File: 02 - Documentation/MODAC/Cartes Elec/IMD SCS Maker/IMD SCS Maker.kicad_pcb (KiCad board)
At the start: 2 copper layers, 32 x 22.4 mm, 12 parts, among them J1 2P Droit 2-11-2022, J3 3P Droit 22-11-2032, Q1 NMOS SQ2348ES-T1_GE3, U1 Alim LP TSR_0.5-2450

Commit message: MAJ 3D Modac
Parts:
- moved J1 2.31 mm to (67.3, 54.4), turned to -90 degrees
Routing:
- net +12V: track 17.2 -> 19.3 mm
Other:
- board text added: "12V"
- board text added: "GND"
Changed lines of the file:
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@@
 			(layer "F.Fab")
 		)
+		(fp_text user "${REFERENCE}"
+			(at -2.54 0 0)
+			(layer "F.Fab")
+			(effects
+				(font
+					(size 1.27 1.27)
+					(thickness 0.254)
+				)
+			)
+		)
 		(pad "1" thru_hole circle
 			(at 3.21 -2)
@@
 			(pintype "passive")
 		)
-		(model "TSR_0.5-2450.stp"
+		(model "${EPSA3D}/TSR_0.5-2450.stp"
 			(offset
 				(xyz -21.61000029 17.88999912 10.24999985)
@@
 			(pintype "passive")
 		)
-		(model "22-11-2032.step"
+		(model "${EPSA3D}/22-11-2032.step"
 			(offset
 				(xyz 2.54 0 1.5)
@@
 	(footprint "EPSA_lib:MOLEX_22-11-2022"
 		(layer "F.Cu")
-		(at 67.3165 56.706 90)
+		(at 67.3165 54.4 -90)
 		(property "Reference" "J1"
-			(at 1.488 -2.1 -90)
+			(at 1.488 -2.1 90)
 			(layer "F.SilkS")
 			(effects
@@
 		)
 		(property "Value" "2P Droit 2-11-2022"
-			(at 7.62 4.615 -90)
+			(at 7.62 4.615 90)
 			(layer "F.Fab")
 			(effects
@@
 		)
 		(property "Footprint" "EPSA_lib:MOLEX_22-11-2022"
-			(at 0 0 90)
+			(at 0 0 -90)
 			(unlocked yes)
 			(layer "F.Fab")
@@
 		)
 		(property "Datasheet" ""
-			(at 0 0 90)
+			(at 0 0 -90)
 			(unlocked yes)
 			(layer "F.Fab")
@@
 		)
 		(property "Description" ""
-			(at 0 0 90)
+			(at 0 0 -90)
 			(unlocked yes)
 			(layer "F.Fab")
@@
 		)
 		(property "Sim.Pins" "1=1 2=2"
-			(at 0 0 90)
+			(at 0 0 -90)
 			(unlocked yes)
 			(layer "F.Fab")
@@
 		)
 		(property "Sim.Device" "SPICE"
-			(at 0 0 90)
+			(at 0 0 -90)
 			(unlocked yes)
 			(layer "F.Fab")
@@
 		)
 		(property "Sim.Params" "type=\"J\" model=\"22-11-2022\" lib=\"\""
-			(at 0 0 90)
+			(at 0 0 -90)
 			(unlocked yes)
 			(layer "F.Fab")
@@
 		)
 		(property "MAXIMUM_PACKAGE_HEIGHT" "10.66mm"
-			(at 0 0 90)
+			(at 0 0 -90)
 			(unlocked yes)
 			(layer "F.Fab")
@@
 		)
 		(property "PARTREV" "BD8"
-			(at 0 0 90)
+			(at 0 0 -90)
 			(unlocked yes)
 			(layer "F.Fab")
@@
 		)
 		(property "STANDARD" "Manufacturer Recommendations"
-			(at 0 0 90)
+			(at 0 0 -90)
 			(unlocked yes)
 			(layer "F.Fab")
@@
 		)
 		(property "MANUFACTURER" "Molex"
-			(at 0 0 90)
+			(at 0 0 -90)
 			(unlocked yes)
 			(layer "F.Fab")
@@
 		)
 		(property "Render Name" "2P Droit"
-			(at 0 0 90)
+			(at 0 0 -90)
 			(unlocked yes)
 			(layer "F.Fab")
@@
 		(attr through_hole)
 		(fp_line
-			(start 3.735 -3.1)
-			(end 3.735 3.25)
+			(start -1.195 3.25)
+			(end -1.195 -3.1)
 			(stroke
 				(width 0.127)
@@
 		)
 		(fp_line
-			(start -1.195 -3.1)
-			(end 3.735 -3.1)
+			(start 3.735 3.25)
+			(end -1.195 3.25)
 			(stroke
 				(width 0.127)
@@
 		)
 		(fp_line
-			(start 3.735 3.25)
-			(end -1.195 3.25)
+			(start -1.195 -3.1)
+			(end 3.735 -3.1)
 			(stroke
 				(width 0.127)
@@
 		)
 		(fp_line
-			(start -1.195 3.25)
-			(end -1.195 -3.1)
+			(start 3.735 -3.1)
+			(end 3.735 3.25)
 			(stroke
 				(width 0.127)
@@
 		)
 		(fp_line
-			(start 3.985 -3.35)
-			(end 3.985 3.5)
+			(start -1.445 3.5)
+			(end -1.445 -3.35)
 			(stroke
 				(width 0.05)
@@
 		)
 		(fp_line
-			(start -1.445 -3.35)
-			(end 3.985 -3.35)
+			(start 3.985 3.5)
+			(end -1.445 3.5)
 			(stroke
 				(width 0.05)
@@
 		)
 		(fp_line
-			(start 3.985 3.5)
-			(end -1.445 3.5)
+			(start -1.445 -3.35)
+			(end 3.985 -3.35)
 			(stroke
 				(width 0.05)
@@
 		)
 		(fp_line
-			(start -1.445 3.5)
-			(end -1.445 -3.35)
+			(start 3.985 -3.35)
+			(end 3.985 3.5)
 			(stroke
 				(width 0.05)
@@
 		)
 		(fp_line
-			(start 3.735 -3.1)
-			(end 3.735 3.25)
+			(start -1.195 3.25)
+			(end -1.195 -3.1)
 			(stroke
 				(width 0.127)
@@
 		)
 		(fp_line
-			(start -1.195 -3.1)
-			(end 3.735 -3.1)
+			(start 3.735 3.25)
+			(end -1.195 3.25)
 			(stroke
 				(width 0.127)
@@
 		)
 		(fp_line
-			(start 3.735 3.25)
-			(end -1.195 3.25)
+			(start -1.195 -3.1)
+			(end 3.735 -3.1)
 			(stroke
 				(width 0.127)
@@
 		)
 		(fp_line
-			(start -1.195 3.25)
-			(end -1.195 -3.1)
+			(start 3.735 -3.1)
+			(end 3.735 3.25)
 			(stroke
 				(width 0.127)
@@
 		)
 		(pad "1" thru_hole rect
-			(at 0 0 90)
+			(at 0 0 270)
 			(size 1.53 1.53)
 			(drill 1.02)
@@
 		)
 		(pad "2" thru_hole circle
-			(at 2.54 0 90)
+			(at 2.54 0 270)
 			(size 1.53 1.53)
 			(drill 1.02)
@@
 			(pintype "passive")
 		)
-		(model "22-11-2022.step"
+		(model "${EPSA3D}/22-11-2022.step"
 			(offset
 				(xyz 1.25 0 1.5)
@@
 			(pintype "passive")
 		)
-		(model "RK73H2BLTDD2152F.stp"
+		(model "${EPSA3D}/RK73H2BLTDD2152F.stp"
 			(offset
 				(xyz 0 0 0)
@@
 			(pintype "passive")
 		)
-		(model "RK73H2BLTDD2152F.stp"
+		(model "${EPSA3D}/RK73H2BLTDD2152F.stp"
 			(offset
 				(xyz 0 0 0)
@@
 			(pintype "passive")
 		)
-		(model "0805Y1000104JXT.stp"
+		(model "${EPSA3D}/0805Y1000104JXT.stp"
 			(offset
 				(xyz 0 0 0)
@@
 		(tags "MOSFET (P-Channel)")
 		(property "Reference" "Q1"
-			(at 1.05 -2.730562 360)
+			(at 1.05 -2.730562 0)
 			(layer "F.SilkS")
 			(effects
@@
 		)
 		(property "Value" "NMOS SQ2348ES-T1_GE3"
-			(at -0.05 5.08 360)
+			(at -0.05 5.08 0)
 			(layer "F.SilkS")
 			(hide yes)
@@
 		)
 		(fp_text user "${REFERENCE}"
-			(at -5.08 0 360)
+			(at -5.08 0 0)
 			(layer "F.Fab")
 			(effects
@@
 			(pintype "passive")
 		)
-		(model "${EPSA}/3Dmodel/SI2343CDS-T1-GE3.stp"
+		(model "${EPSA3D}/SI2343CDS-T1-GE3.stp"
 			(offset
 				(xyz 0 0 0)
@@
 			(pintype "passive")
 		)
-		(model "RK73H2BLTDD2152F.stp"
+		(model "${EPSA3D}/RK73H2BLTDD2152F.stp"
 			(offset
 				(xyz 0 0 0)
@@
 		(layer "Edge.Cuts")
 	)
+	(gr_text "GND"
+		(at 64.2 53 0)
+		(layer "F.SilkS")
+		(effects
+			(font
+				(size 0.7 0.7)
+				(thickness 0.175)
+				(bold yes)
+			)
+			(justify left bottom)
+		)
+	)
 	(gr_text "SCS Maker V1.0 EPSA"
 		(at 67.7565 60.96 0)
@@
 		)
 	)
+	(gr_text "12V"
+		(at 64.2 59.4 0)
+		(layer "F.SilkS")
+		(effects
+			(font
+				(size 0.7 0.7)
+				(thickness 0.175)
+				(bold yes)
+			)
+			(justify left bottom)
+		)
+	)
 	(segment
-		(start 67.595388 56.427112)
-		(end 67.3165 56.706)
+		(start 67.3165 54.166)
+		(end 67.7605 54.61)
 		(width 0.25)
 		(layer "F.Cu")
@@
 	)
 	(segment
-		(start 75.193612 54.61)
+		(start 71.572888 54.427112)
 		(end 75.3765 54.427112)
 		(width 0.25)
@@
 	)
 	(segment
-		(start 67.7605 54.61)
-		(end 75.193612 54.61)
+		(start 67.595388 56.427112)
+		(end 67.3165 56.706)
 		(width 0.25)
 		(layer "F.Cu")
@@
 	)
 	(segment
-		(start 67.3165 52.5715)
-		(end 70.866 49.022)
+		(start 67.3165 56.94)
+		(end 69.06 56.94)
 		(width 0.25)
 		(layer "F.Cu")
@@
 	)
 	(segment
-		(start 67.3165 54.166)
-		(end 67.7605 54.61)
+		(start 75.193612 54.61)
+		(end 75.3765 54.427112)
 		(width 0.25)
 		(layer "F.Cu")
@@
 	)
 	(segment
-		(start 70.866 49.022)
-		(end 70.866 46.736)
+		(start 69.06 56.94)
+		(end 71.572888 54.427112)
 		(width 0.25)
 		(layer "F.Cu")
@@
 	)
 	(segment
-		(start 67.3165 54.166)
-		(end 67.3165 52.5715)
+		(start 70.866 49.916612)
+		(end 75.3765 54.427112)
+		(width 0.25)
+		(layer "F.Cu")
+		(net 2)
+	)
+	(segment
+		(start 70.866 46.736)
+		(end 70.866 49.916612)
 		(width 0.25)
 		(layer "F.Cu")

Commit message: Prise en compte retours JDL
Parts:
- removed Q1: NMOS SQ2348ES-T1_GE3, EPSA_lib:SOT95P237X112-3N
- added CP1: Comparator, Package_TO_SOT_SMD:SOT-353_SC-70-5, F.Cu at (82.0, 55.0)
- added R4: 1k, EPSA_lib:RESC3216X70N, F.Cu at (81.0, 58.0)
- added R5: 1k, EPSA_lib:RESC3216X70N, F.Cu at (93.5, 48.0)
- added R6: 2k, EPSA_lib:RESC3216X70N, F.Cu at (82.0, 51.0)
- added R7: 1k, EPSA_lib:RESC3216X70N, F.Cu at (91.0, 48.0)
- moved R1 2.75 mm to (87.5, 51.5)
- moved R2 2.73 mm to (87.5, 54.2)
- moved R3 2.73 mm to (87.5, 57.2)
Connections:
- R1 pad 2: /Sensor Output -> Net-(CP1-Pad4)
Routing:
- net GND: track 0.72 -> 29.9 mm, vias 0 -> 4
- net Net-(CP1--): track 0.00 -> 23.0 mm, vias 0 -> 2
- net Net-(CP1-+): track 0.00 -> 16.0 mm, vias 0 -> 2
- net /PDU: track 8.53 -> 0.00 mm
- net Net-(CP1-Pad4): track 0.00 -> 5.39 mm
- net /Output SCS: track 18.8 -> 15.4 mm
- net +5V: track 11.5 -> 10.6 mm
- added copper zone on F.Cu, net +5V
- added copper zone on B.Cu, net GND
- removed copper zone on F.Cu, net GND
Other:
- board text added: "IMD SCS Maker V1.0 EPSA"
- board text removed: "SCS Maker V1.0 EPSA"

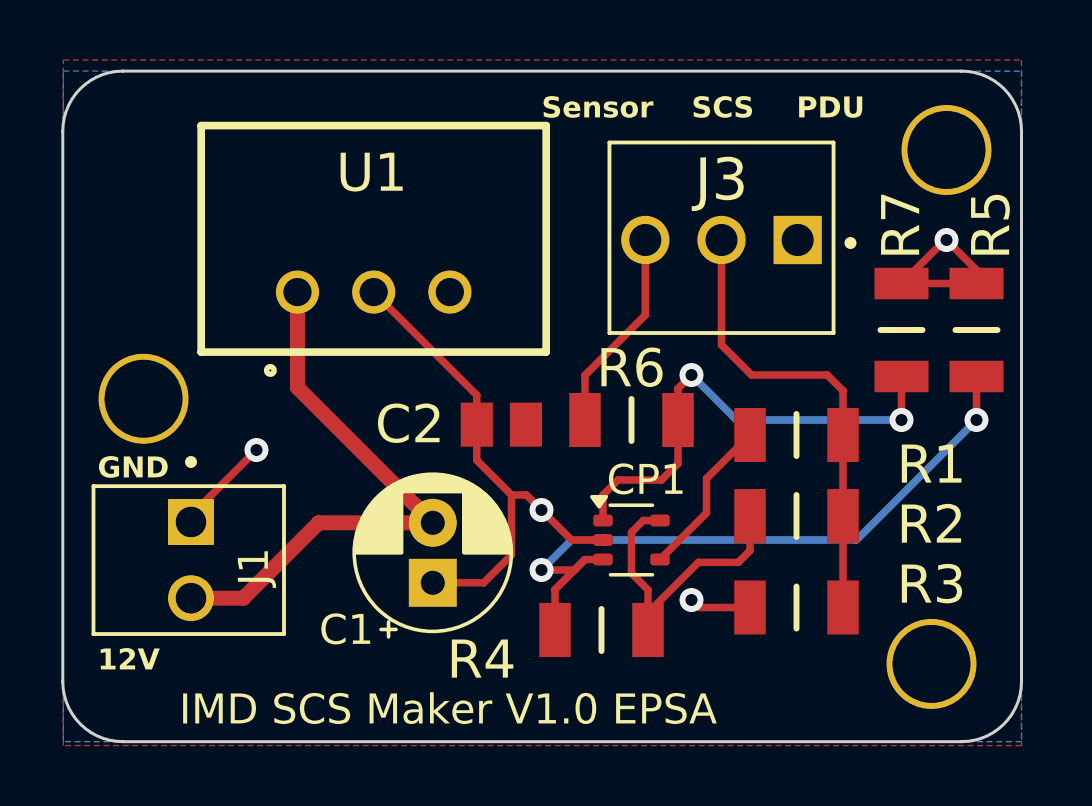
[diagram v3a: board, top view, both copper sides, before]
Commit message: Modif cartes, ajout ventilateur et placement 3D PCB
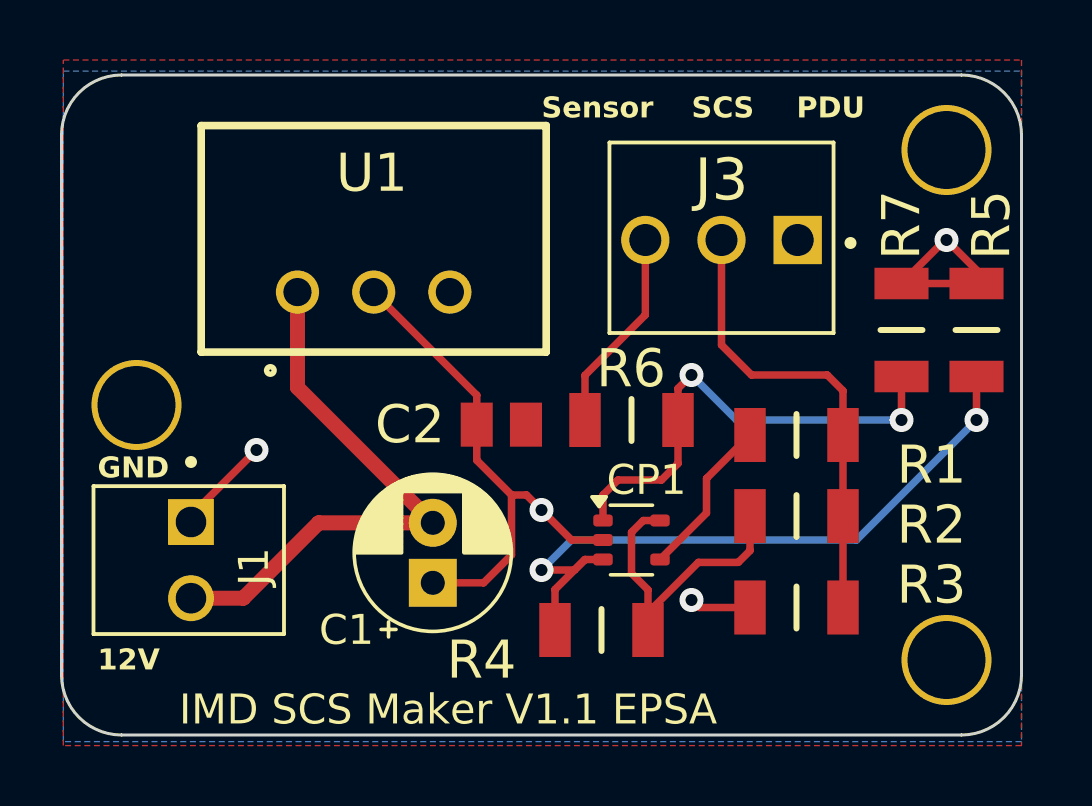
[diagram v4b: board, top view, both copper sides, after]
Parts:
- moved ? 0.52 mm to (92.5, 59.0)
- moved ? 0.31 mm to (65.5, 50.5)
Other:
- board size 32 x 22.4 mm -> 32 x 22 mm
- board text added: "IMD SCS Maker V1.1 EPSA"
- board text removed: "IMD SCS Maker V1.0 EPSA"
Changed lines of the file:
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@@
 	(footprint ""
 		(layer "F.Cu")
-		(at 92 59.1312)
+		(at 92.5 59)
 		(property "Reference" ""
 			(at 0 0 0)
@@
 	(footprint ""
 		(layer "F.Cu")
-		(at 65.7352 50.292)
+		(at 65.5 50.5)
 		(property "Reference" ""
 			(at 0 0 0)
@@
 	)
 	(gr_arc
-		(start 93 39.37)
-		(mid 94.414214 39.955786)
-		(end 95 41.37)
+		(start 93 39.5)
+		(mid 94.414214 40.085786)
+		(end 95 41.5)
 		(stroke
 			(width 0.1)
@@
 	)
 	(gr_arc
-		(start 63.0428 41.37)
-		(mid 63.628586 39.955786)
-		(end 65.0428 39.37)
+		(start 63 41.5)
+		(mid 63.585786 40.085786)
+		(end 65 39.5)
 		(stroke
 			(width 0.1)
@@
 	)
 	(gr_line
-		(start 95 41.37)
-		(end 95 59.722)
+		(start 95 41.5)
+		(end 95 59.5)
 		(stroke
 			(width 0.1)
@@
 		(layer "Edge.Cuts")
 	)
-	(gr_arc
-		(start 65.0428 61.722)
-		(mid 63.628586 61.136214)
-		(end 63.0428 59.722)
+	(gr_line
+		(start 65 39.5)
+		(end 93 39.5)
 		(stroke
 			(width 0.1)
@@
 	)
 	(gr_line
-		(start 65.0428 39.37)
-		(end 93 39.37)
+		(start 93 61.5)
+		(end 65 61.5)
 		(stroke
 			(width 0.1)
@@
 		(layer "Edge.Cuts")
 	)
-	(gr_line
-		(start 93 61.722)
-		(end 65.0428 61.722)
+	(gr_arc
+		(start 65 61.5)
+		(mid 63.585786 60.914214)
+		(end 63 59.5)
 		(stroke
 			(width 0.1)
@@
 		(layer "Edge.Cuts")
 	)
-	(gr_line
-		(start 63.0428 59.722)
-		(end 63.0428 41.37)
+	(gr_arc
+		(start 95 59.5)
+		(mid 94.414214 60.914214)
+		(end 93 61.5)
 		(stroke
 			(width 0.1)
@@
 		(layer "Edge.Cuts")
 	)
-	(gr_arc
-		(start 95 59.722)
-		(mid 94.414214 61.136214)
-		(end 93 61.722)
+	(gr_line
+		(start 63 59.5)
+		(end 63 41.5)
 		(stroke
 			(width 0.1)
@@
 		)
 	)
-	(gr_text "IMD SCS Maker V1.0 EPSA"
+	(gr_text "IMD SCS Maker V1.1 EPSA"
 		(at 66.919472 61.237478 0)
 		(layer "F.SilkS")
